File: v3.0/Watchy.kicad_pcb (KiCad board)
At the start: 2 copper layers, 33.8 x 46 mm, 78 parts, among them J1 FPC24(0.5MM), J2 Conn_01x06, J3 Battery, J5 Conn_01x06, M1 Vibration_Motor, Q1 AO3400A, Q4 CJ2301, Q5 S8050, SW1 BTN, SW2 BTN, SW3 BTN, SW4 BTN, U1 CH340X, U2 ME6211C33M5G-N, U3 USBLC6-2P6, U4 BMA423, U5 TP4054, U6 PCF8563BS, U7 ESP32-S3, U8 SR2HARU, Y1 32.768KHz, Y3 40MHZ

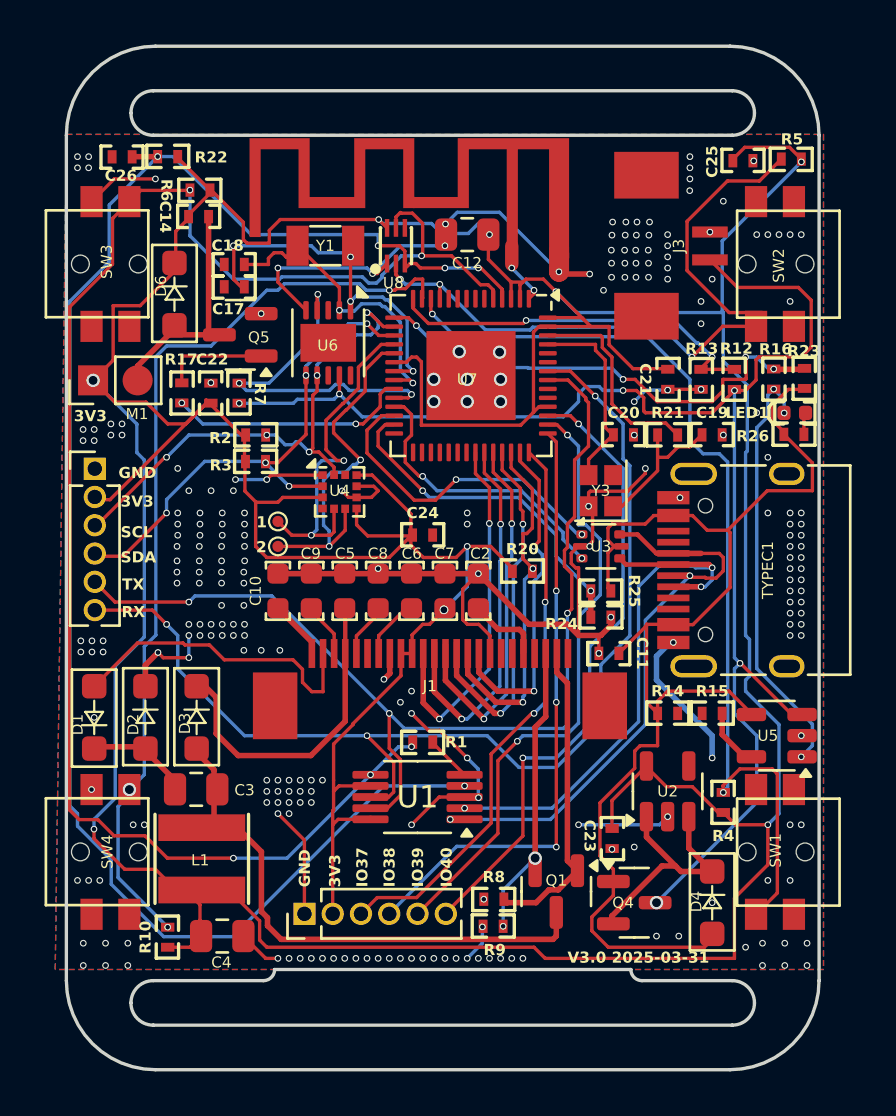
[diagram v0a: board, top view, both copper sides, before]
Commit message: change ch340x position
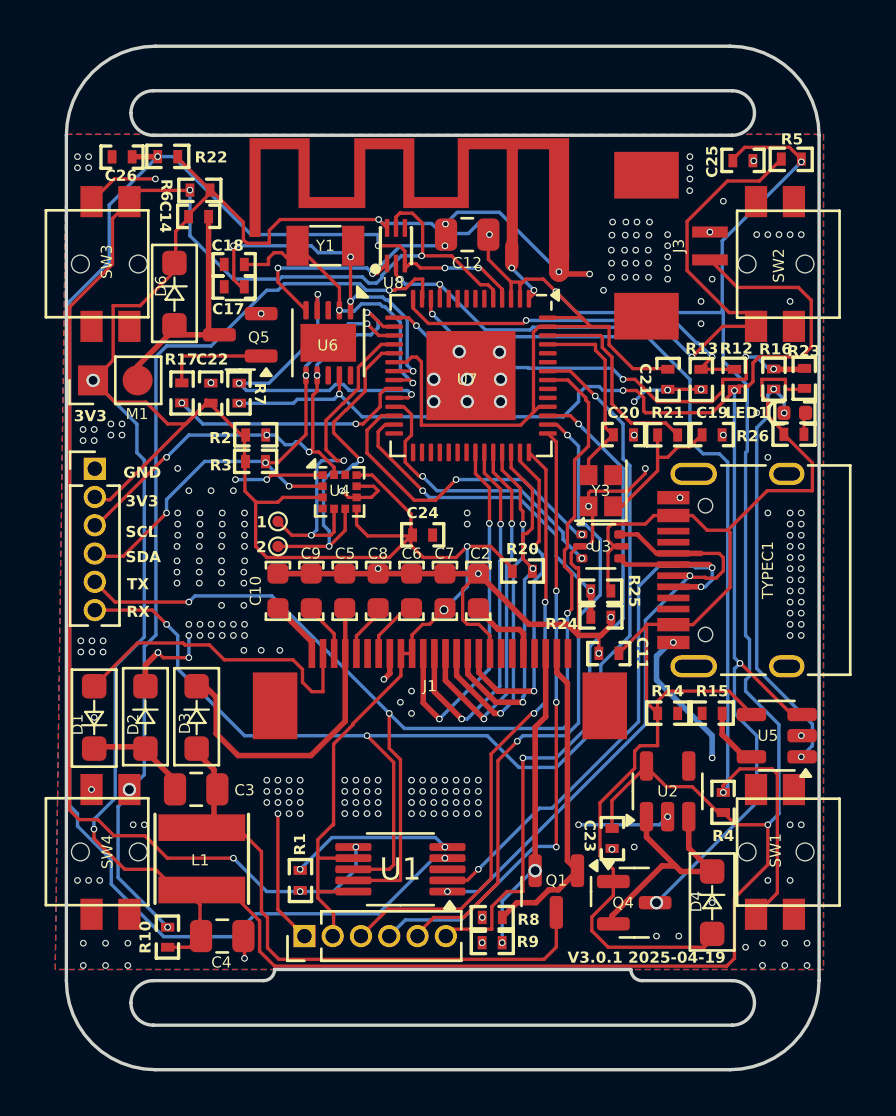
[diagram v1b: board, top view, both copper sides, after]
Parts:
- moved R1 8.30 mm to (79.2, 107.6), turned to -90 degrees
- moved U1 3.33 mm to (83.7, 107.1)
- moved J2 1.00 mm to (79.4, 110.1)
- moved R8 0.82 mm to (87.8, 109.3)
- moved R9 0.74 mm to (87.8, 110.4)
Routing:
- net GND: track 100.4 -> 90.5 mm, vias 257 -> 273
- net Net-(U1-~{CTS}): track 2.06 -> 7.27 mm, vias 0 -> 2
- net TX: track 47.1 -> 51.5 mm
- net RX: track 50.0 -> 54.0 mm
- net BTN_3: track 71.4 -> 68.8 mm
- net IO40: track 28.7 -> 31.1 mm
- net EN: track 74.9 -> 72.7 mm
- net DN: track 25.7 -> 27.8 mm
- net VBUS: track 56.7 -> 58.7 mm
- net IO37: track 25.6 -> 27.5 mm
- net IO39: track 27.9 -> 29.7 mm
- net +3V3: track 248.9 -> 250.7 mm
- net Net-(D3-A): track 25.6 -> 27.2 mm
- net DP: track 25.8 -> 27.3 mm
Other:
- board text added: "V3.0.1 2025-04-19"
- board text removed: "V3.0 2025-03-31"
